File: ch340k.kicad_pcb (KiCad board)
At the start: 2 copper layers, 33 x 17.8 mm, 8 parts, among them J1 USB_B_Mini, J2 Conn_01x06_Male, U1 CH340K

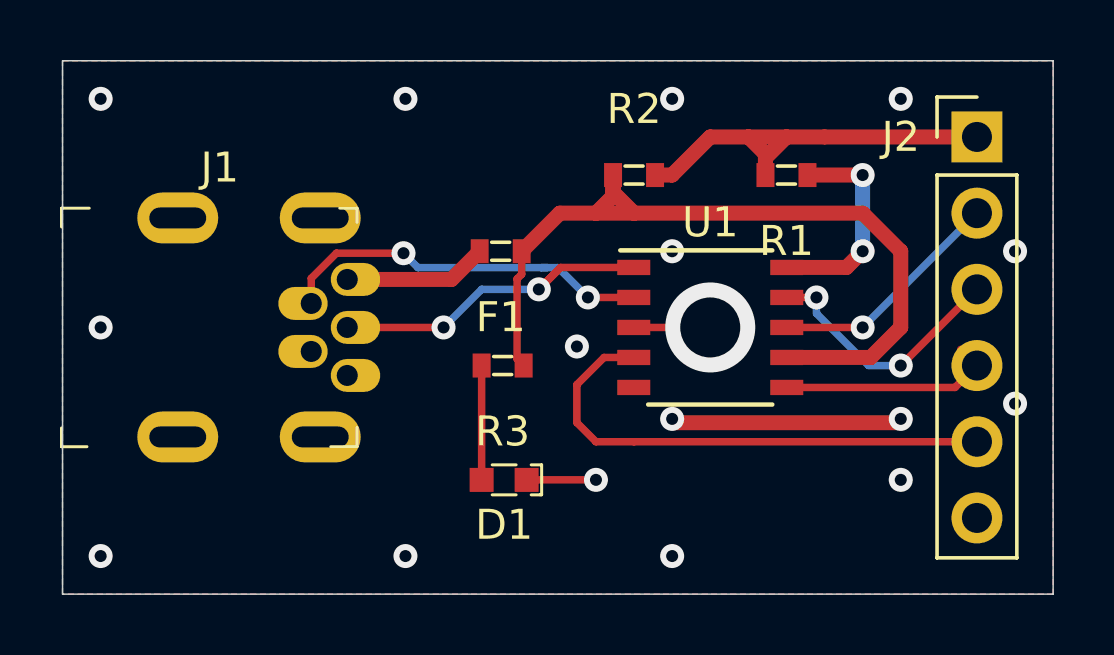
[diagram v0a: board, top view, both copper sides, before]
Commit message: M5Stamp/ESP32 Downloader prototype
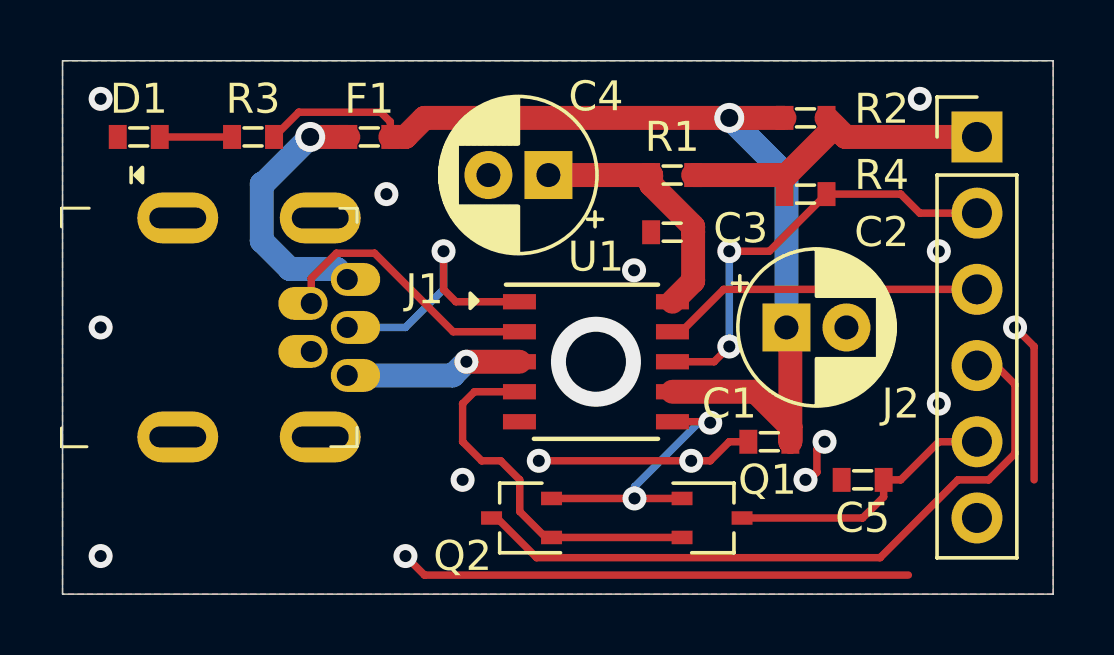
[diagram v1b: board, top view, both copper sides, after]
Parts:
- added C1: 0.1u, UserLib:0603, F.Cu at (137.9, 78.7)
- added C2: 10u, Capacitor_THT:CP_Radial_D5.0mm_P2.00mm, F.Cu at (138.4, 74.9)
- added C3: 0.1u, UserLib:0603, F.Cu at (134.6, 71.8)
- added C4: 10u, Capacitor_THT:CP_Radial_D5.0mm_P2.00mm, F.Cu at (130.5, 69.8)
- added C5: 0.1u, UserLib:0603, F.Cu at (141.0, 80.0)
- added Q1: SSM3K7002BFU, Package_TO_SOT_SMD:SOT-323_SC-70, F.Cu at (135.9, 81.3)
- added Q2: SSM3K7002BFU, Package_TO_SOT_SMD:SOT-323_SC-70, F.Cu at (129.6, 81.3)
- added R4: 2.2k, UserLib:0603, F.Cu at (139.1, 70.5)
- D1: footprint digikey-footprints:LED_2-SMD_No_Lead_1.7x0.8mm -> UserLib:0603
- F1, R1, R2: footprint digikey-footprints:0603 -> UserLib:0603
- R3: value 10k -> 1k; footprint digikey-footprints:0603 -> UserLib:0603
- moved D1 16.7 mm to (116.8, 68.6), turned to 0 degrees
- moved R3 11.3 mm to (120.7, 68.6)
- moved R2 6.02 mm to (139.1, 67.9)
- moved F1 5.81 mm to (124.5, 68.6)
- moved U1 3.98 mm to (132.1, 76.1)
- moved R1 3.81 mm to (134.6, 69.8), turned to 0 degrees
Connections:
- J1 pad 4: Net-(J1-Pad4) -> unconnected-(J1-Pad4)
- U1 pad 4: Net-(J2-Pad5) -> Net-(U1-Pad4)
- U1 pad 5: Net-(U1-Pad5) -> unconnected-(U1-Pad5)
- U1 pad 6: Net-(J2-Pad4) -> Net-(Q1-Pad1)
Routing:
- net GND: track 13.4 -> 37.2 mm
- net Net-(J2-Pad4): track 7.41 -> 23.3 mm
- net Net-(U1-Pad4): track 0.00 -> 12.3 mm
- net Net-(Q1-Pad1): track 0.00 -> 8.76 mm, vias 0 -> 2
- net Net-(J2-Pad5): track 17.1 -> 8.89 mm
- net Net-(F1-Pad1): track 27.7 -> 34.8 mm, vias 0 -> 1
- net Net-(J2-Pad2): track 7.92 -> 14.6 mm, vias 1 -> 2
- net Net-(F1-Pad2): track 4.80 -> 8.75 mm, vias 0 -> 1
- net Net-(J2-Pad1): track 14.3 -> 10.7 mm
- net Net-(J1-Pad2): track 12.7 -> 9.21 mm, vias 2 -> 0
- net Net-(J1-Pad3): track 11.3 -> 8.98 mm, vias 2 -> 1
- net Net-(J2-Pad3): track 8.64 -> 10.7 mm, vias 2 -> 0
- net Net-(D1-Pad2): track 3.81 -> 2.41 mm
- net Net-(R1-Pad1): track 7.13 -> 8.51 mm, vias 2 -> 0
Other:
- board text added: "3.3V"
- board text added: "BT"
- board text added: "CH340K"
- board text added: "EN"
- board text added: "GND"
- board text added: "JK1MLY 2022.3"
- board text added: "RXD"
- board text added: "TXD"
